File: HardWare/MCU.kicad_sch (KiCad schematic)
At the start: 45 parts, among them J1 复用Typec, U1 STM32F415RGTx, U3 LP5907MFX-3.3, U4 RT9193, Y1 8M

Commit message: Add PCB
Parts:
- removed J?: SPI_conn, symbol Connector_Generic:Conn_01x06
- added J9: SPI_conn, Connector_Molex:Molex_CLIK-Mate_502386-0670_1x06-1MP_P1.25mm_Horizontal, symbol Connector_Generic_MountingPin:Conn_01x06_MountingPin
- D3: footprint (none) -> Diode_SMD:D_0805_2012Metric
- J6: renamed from J?; footprint (none) -> Connector_PinSocket_2.54mm:PinSocket_1x05_P2.54mm_Horizontal
- J7: renamed from J?; footprint (none) -> USER:XT30U-M
- J8: renamed from J?; footprint (none) -> Connector_Molex:Molex_CLIK-Mate_502443-0270_1x02-1MP_P2.00mm_Vertical
- U4: footprint (none) -> Package_TO_SOT_SMD:SOT-23-5
- U6: renamed from U?; footprint (none) -> Package_SO:SOP-8_3.9x4.9mm_P1.27mm
- gave numbers to parts that had none: 12
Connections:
- net +3V3: now also J9.1 (Pin_1)
- net GND: now also J9.6 (Pin_6)
- net SPI_MISO: now also J9.4 (Pin_4)
- net SPI_MOSI: now also J9.5 (Pin_5)
- net SPI_SCK: now also J9.3 (Pin_3)
- net EXSPI_CS: now reaches U1.50 (PA15)
- net EXSPI_CS: now also J9.2 (Pin_2)
- no-connect marks 7 -> 8

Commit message: Add Rules
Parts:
- J6: footprint Connector_PinSocket_2.54mm:PinSocket_1x05_P2.54mm_Horizontal -> Connector_PinSocket_2.54mm:PinSocket_1x05_P2.54mm_Vertical
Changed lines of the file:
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@@
     (property "Reference" "J6" (id 0) (at 25.4 85.09 0))
     (property "Value" "SWD" (id 1) (at 25.4 87.63 0))
-    (property "Footprint" "Connector_PinSocket_2.54mm:PinSocket_1x05_P2.54mm_Horizontal" (id 2) (at 25.4 96.52 0)
+    (property "Footprint" "Connector_PinSocket_2.54mm:PinSocket_1x05_P2.54mm_Vertical" (id 2) (at 25.4 96.52 0)
       (effects (font (size 1.27 1.27)) hide)
     )
@@
   (symbol (lib_id "Device:R") (at 182.88 100.33 90) (unit 1)
     (in_bom yes) (on_board yes)
-    (property "Reference" "R51" (id 0) (at 182.88 97.79 90))
+    (property "Reference" "R51" (id 0) (at 182.88 102.87 90))
     (property "Value" "22" (id 1) (at 182.88 100.33 90))
     (property "Footprint" "Resistor_SMD:R_0603_1608Metric" (id 2) (at 182.88 102.108 90)

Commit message: 修改一些BUG
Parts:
- C53, C54, C55, C57, C58, C59, C60, C61: value 47uf -> 10uf; footprint Capacitor_SMD:C_1812_4532Metric -> Capacitor_SMD:C_1210_3225Metric
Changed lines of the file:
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@@
     (in_bom yes) (on_board yes)
     (property "Reference" "C53" (id 0) (at 209.55 147.32 0))
-    (property "Value" "47uf" (id 1) (at 214.63 152.4 0))
-    (property "Footprint" "Capacitor_SMD:C_1812_4532Metric" (id 2) (at 213.0552 153.67 0)
+    (property "Value" "10uf" (id 1) (at 214.63 152.4 0))
+    (property "Footprint" "Capacitor_SMD:C_1210_3225Metric" (id 2) (at 213.0552 153.67 0)
       (effects (font (size 1.27 1.27)) hide)
     )
@@
     (in_bom yes) (on_board yes)
     (property "Reference" "C54" (id 0) (at 218.44 147.32 0))
-    (property "Value" "47uf" (id 1) (at 223.52 152.4 0))
-    (property "Footprint" "Capacitor_SMD:C_1812_4532Metric" (id 2) (at 221.9452 153.67 0)
+    (property "Value" "10uf" (id 1) (at 223.52 152.4 0))
+    (property "Footprint" "Capacitor_SMD:C_1210_3225Metric" (id 2) (at 221.9452 153.67 0)
       (effects (font (size 1.27 1.27)) hide)
     )
@@
     (in_bom yes) (on_board yes)
     (property "Reference" "C55" (id 0) (at 227.33 147.32 0))
-    (property "Value" "47uf" (id 1) (at 232.41 152.4 0))
-    (property "Footprint" "Capacitor_SMD:C_1812_4532Metric" (id 2) (at 230.8352 153.67 0)
+    (property "Value" "10uf" (id 1) (at 232.41 152.4 0))
+    (property "Footprint" "Capacitor_SMD:C_1210_3225Metric" (id 2) (at 230.8352 153.67 0)
       (effects (font (size 1.27 1.27)) hide)
     )
@@
     (in_bom yes) (on_board yes)
     (property "Reference" "C57" (id 0) (at 236.22 147.32 0))
-    (property "Value" "47uf" (id 1) (at 241.3 152.4 0))
-    (property "Footprint" "Capacitor_SMD:C_1812_4532Metric" (id 2) (at 239.7252 153.67 0)
+    (property "Value" "10uf" (id 1) (at 241.3 152.4 0))
+    (property "Footprint" "Capacitor_SMD:C_1210_3225Metric" (id 2) (at 239.7252 153.67 0)
       (effects (font (size 1.27 1.27)) hide)
     )
@@
     (in_bom yes) (on_board yes)
     (property "Reference" "C58" (id 0) (at 245.11 147.32 0))
-    (property "Value" "47uf" (id 1) (at 250.19 152.4 0))
-    (property "Footprint" "Capacitor_SMD:C_1812_4532Metric" (id 2) (at 248.6152 153.67 0)
+    (property "Value" "10uf" (id 1) (at 250.19 152.4 0))
+    (property "Footprint" "Capacitor_SMD:C_1210_3225Metric" (id 2) (at 248.6152 153.67 0)
       (effects (font (size 1.27 1.27)) hide)
     )
@@
     (in_bom yes) (on_board yes)
     (property "Reference" "C61" (id 0) (at 269.24 147.32 0))
-    (property "Value" "47uf" (id 1) (at 274.32 152.4 0))
-    (property "Footprint" "Capacitor_SMD:C_1812_4532Metric" (id 2) (at 272.7452 153.67 0)
+    (property "Value" "10uf" (id 1) (at 274.32 152.4 0))
+    (property "Footprint" "Capacitor_SMD:C_1210_3225Metric" (id 2) (at 272.7452 153.67 0)
       (effects (font (size 1.27 1.27)) hide)
     )
@@
     (in_bom yes) (on_board yes)
     (property "Reference" "C59" (id 0) (at 252.73 147.32 0))
-    (property "Value" "47uf" (id 1) (at 257.81 152.4 0))
-    (property "Footprint" "Capacitor_SMD:C_1812_4532Metric" (id 2) (at 256.2352 153.67 0)
+    (property "Value" "10uf" (id 1) (at 257.81 152.4 0))
+    (property "Footprint" "Capacitor_SMD:C_1210_3225Metric" (id 2) (at 256.2352 153.67 0)
       (effects (font (size 1.27 1.27)) hide)
     )
@@
     (in_bom yes) (on_board yes)
     (property "Reference" "C60" (id 0) (at 261.62 147.32 0))
-    (property "Value" "47uf" (id 1) (at 266.7 152.4 0))
-    (property "Footprint" "Capacitor_SMD:C_1812_4532Metric" (id 2) (at 265.1252 153.67 0)
-      (effects (font (size 1.27 1.27)) hide)
-    )
+    (property "Value" "10uf" (id 1) (at 266.7 152.4 0))
+    (property "Footprint" "Capacitor_SMD:C_1210_3225Metric" (id 2) (at 265.1252 153.67 0)
+      (effects (font (size 1.27 1.27)) hide)
+    )

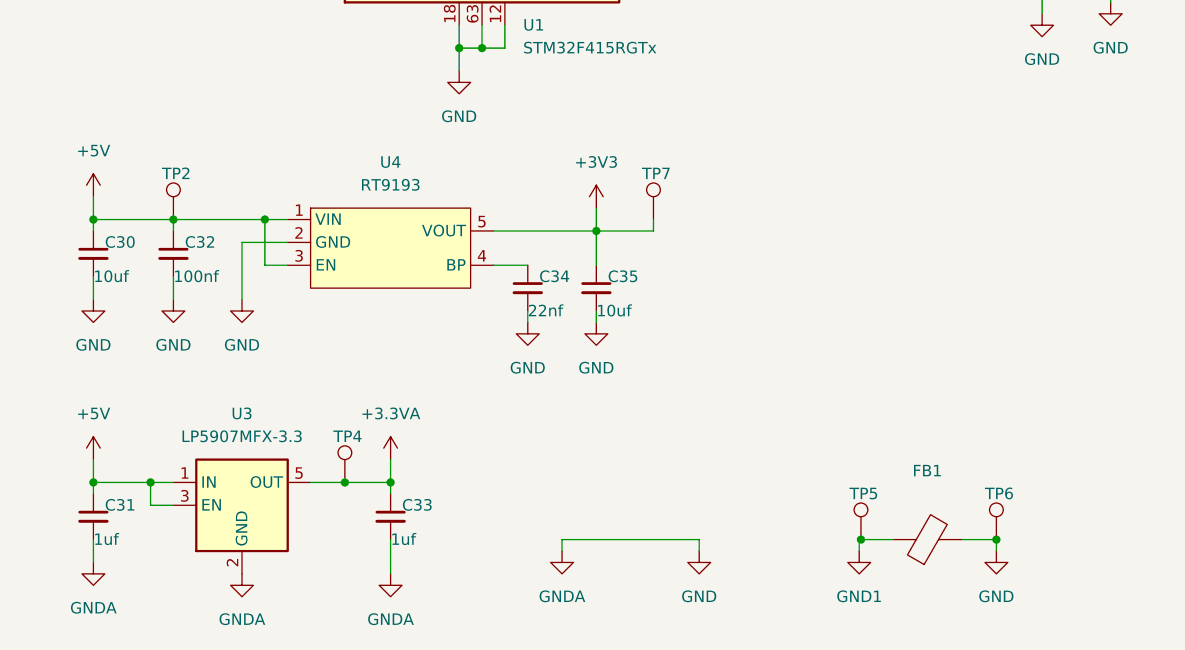
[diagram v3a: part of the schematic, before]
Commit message: 更新一些信号电源
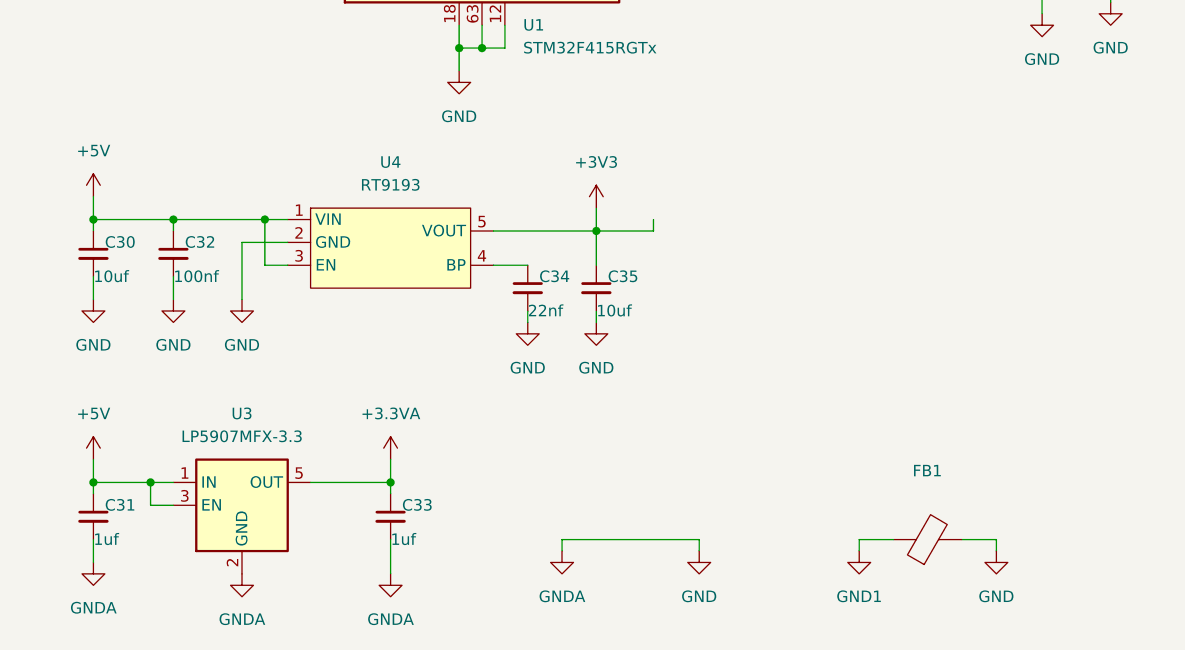
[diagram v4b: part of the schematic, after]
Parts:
- removed TP2, TP4, TP5, TP6, TP7: TP, TestPoint:TestPoint_THTPad_D2.0mm_Drill1.0mm, symbol Connector:TestPoint
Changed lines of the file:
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@@
   (junction (at 238.76 154.94) (diameter 0) (color 0 0 0 0)
   )
-  (junction (at 77.47 172.72) (diameter 0) (color 0 0 0 0)
-  )
   (junction (at 271.78 154.94) (diameter 0) (color 0 0 0 0)
   )
@@
   (junction (at 229.87 144.78) (diameter 0) (color 0 0 0 0)
   )
-  (junction (at 149.86 179.07) (diameter 0) (color 0 0 0 0)
-  )
   (junction (at 212.09 154.94) (diameter 0) (color 0 0 0 0)
   )
@@
   )
   (junction (at 52.07 55.88) (diameter 0) (color 0 0 0 0)
-  )
-  (junction (at 134.8122 179.07) (diameter 0) (color 0 0 0 0)
   )
   (junction (at 49.53 143.51) (diameter 0) (color 0 0 0 0)
@@
     (stroke (width 0) (type default) (color 0 0 0 0))
   )
-  (wire (pts (xy 134.8122 179.07) (xy 138.43 179.07))
-    (stroke (width 0) (type default) (color 0 0 0 0))
-  )
   (wire (pts (xy 71.12 146.05) (xy 66.04 146.05))
     (stroke (width 0) (type default) (color 0 0 0 0))
@@
     (stroke (width 0) (type default) (color 0 0 0 0))
   )
-  (wire (pts (xy 134.62 179.07) (xy 134.8122 179.07))
+  (wire (pts (xy 134.62 179.07) (xy 138.43 179.07))
     (stroke (width 0) (type default) (color 0 0 0 0))
   )
@@
     (stroke (width 0) (type default) (color 0 0 0 0))
   )
-  (wire (pts (xy 82.55 172.72) (xy 77.47 172.72))
-    (stroke (width 0) (type default) (color 0 0 0 0))
-  )
   (wire (pts (xy 105.41 142.24) (xy 105.41 144.78))
     (stroke (width 0) (type default) (color 0 0 0 0))
@@
     (stroke (width 0) (type default) (color 0 0 0 0))
   )
-  (wire (pts (xy 77.47 172.72) (xy 73.66 172.72))
+  (wire (pts (xy 73.66 172.72) (xy 82.55 172.72))
     (stroke (width 0) (type default) (color 0 0 0 0))
   )
@@
     (pin "1")
   )
-  (symbol (lib_id "Connector:TestPoint") (at 149.86 179.07 0) (unit 1)
-    (in_bom yes) (on_board yes)
-    (property "Reference" "TP6" (id 0) (at 148.59 173.99 0)
-      (effects (font (size 1.27 1.27)) (justify left))
-    )
-    (property "Value" "TP" (id 1) (at 149.86 173.99 90)
-      (effects (font (size 1.27 1.27)) (justify left) hide)
-    )
-    (property "Footprint" "TestPoint:TestPoint_THTPad_D2.0mm_Drill1.0mm" (id 2) (at 154.94 179.07 0)
-      (effects (font (size 1.27 1.27)) hide)
-    )
-    (property "Datasheet" "~" (id 3) (at 154.94 179.07 0)
-      (effects (font (size 1.27 1.27)) hide)
-    )
-    (pin "1")
-  )
   (symbol (lib_id "power:+3V3") (at 87.63 25.4 0) (unit 1)
     (in_bom yes) (on_board yes) (fields_autoplaced)
@@
     (pin "2")
   )
-  (symbol (lib_id "Connector:TestPoint") (at 111.76 143.51 0) (unit 1)
-    (in_bom yes) (on_board yes)
-    (property "Reference" "TP7" (id 0) (at 110.49 138.43 0)
-      (effects (font (size 1.27 1.27)) (justify left))
-    )
-    (property "Value" "TP" (id 1) (at 111.76 138.43 90)
-      (effects (font (size 1.27 1.27)) (justify left) hide)
-    )
-    (property "Footprint" "TestPoint:TestPoint_THTPad_D2.0mm_Drill1.0mm" (id 2) (at 116.84 143.51 0)
-      (effects (font (size 1.27 1.27)) hide)
-    )
-    (property "Datasheet" "~" (id 3) (at 116.84 143.51 0)
-      (effects (font (size 1.27 1.27)) hide)
-    )
-    (pin "1")
-  )
-  (symbol (lib_id "Connector:TestPoint") (at 77.47 172.72 0) (unit 1)
-    (in_bom yes) (on_board yes)
-    (property "Reference" "TP4" (id 0) (at 76.2 167.64 0)
-      (effects (font (size 1.27 1.27)) (justify left))
-    )
-    (property "Value" "TP" (id 1) (at 77.47 167.64 90)
-      (effects (font (size 1.27 1.27)) (justify left) hide)
-    )
-    (property "Footprint" "TestPoint:TestPoint_THTPad_D2.0mm_Drill1.0mm" (id 2) (at 82.55 172.72 0)
-      (effects (font (size 1.27 1.27)) hide)
-    )
-    (property "Datasheet" "~" (id 3) (at 82.55 172.72 0)
-      (effects (font (size 1.27 1.27)) hide)
-    )
-    (pin "1")
-  )
   (symbol (lib_id "power:+5V") (at 187.96 76.2 0) (unit 1)
     (in_bom yes) (on_board yes) (fields_autoplaced)
@@
     (pin "2")
   )
-  (symbol (lib_id "Connector:TestPoint") (at 134.8122 179.07 0) (unit 1)
-    (in_bom yes) (on_board yes)
-    (property "Reference" "TP5" (id 0) (at 133.5422 173.99 0)
-      (effects (font (size 1.27 1.27)) (justify left))
-    )
-    (property "Value" "TP" (id 1) (at 134.8122 173.99 90)
-      (effects (font (size 1.27 1.27)) (justify left) hide)
-    )
-    (property "Footprint" "TestPoint:TestPoint_THTPad_D2.0mm_Drill1.0mm" (id 2) (at 139.8922 179.07 0)
-      (effects (font (size 1.27 1.27)) hide)
-    )
-    (property "Datasheet" "~" (id 3) (at 139.8922 179.07 0)
-      (effects (font (size 1.27 1.27)) hide)
-    )
-    (pin "1")
-  )
   (symbol (lib_id "power:GND") (at 198.12 107.95 0) (unit 1)
     (in_bom yes) (on_board yes) (fields_autoplaced)
@@
     (pin "2")
   )
-  (symbol (lib_id "Connector:TestPoint") (at 58.42 143.51 0) (unit 1)
-    (in_bom yes) (on_board yes)
-    (property "Reference" "TP2" (id 0) (at 57.15 138.43 0)
-      (effects (font (size 1.27 1.27)) (justify left))
-    )
-    (property "Value" "TP" (id 1) (at 58.42 138.43 90)
-      (effects (font (size 1.27 1.27)) (justify left) hide)
-    )
-    (property "Footprint" "TestPoint:TestPoint_THTPad_D2.0mm_Drill1.0mm" (id 2) (at 63.5 143.51 0)
-      (effects (font (size 1.27 1.27)) hide)
-    )
-    (property "Datasheet" "~" (id 3) (at 63.5 143.51 0)
-      (effects (font (size 1.27 1.27)) hide)
-    )
-    (pin "1")
-  )
   (symbol (lib_id "power:+3V3") (at 229.87 29.21 0) (unit 1)
